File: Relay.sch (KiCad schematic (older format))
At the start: 9 parts

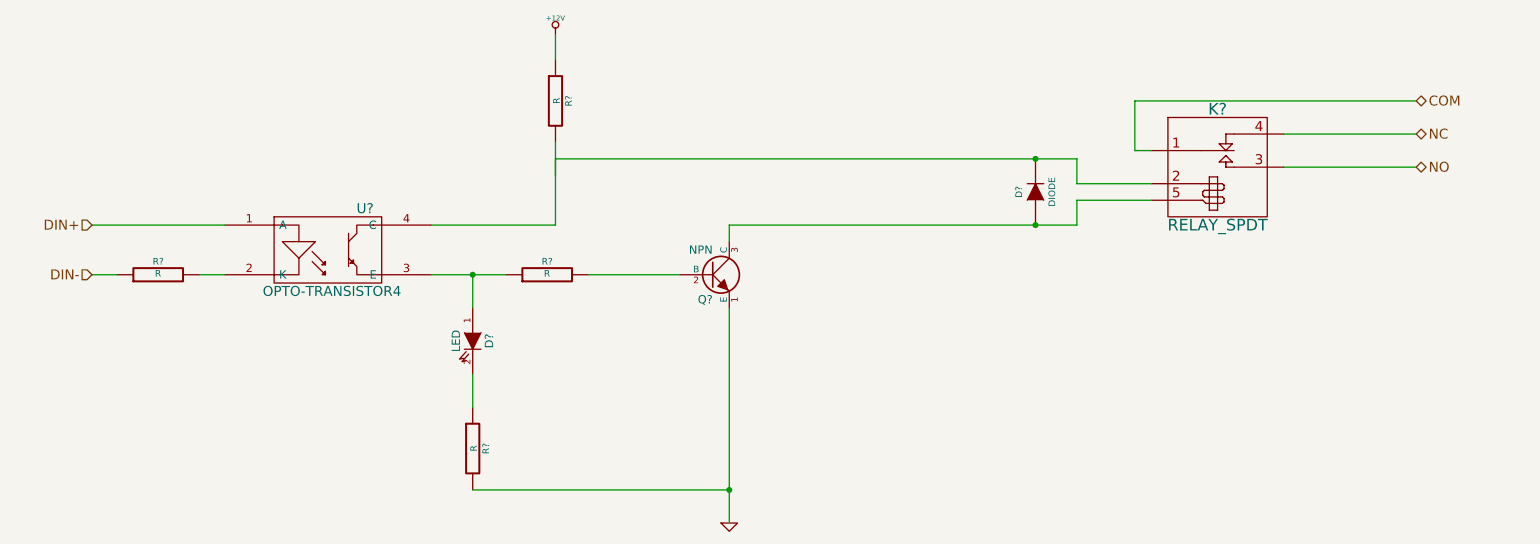
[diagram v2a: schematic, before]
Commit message: 3.9 Understanding The Arduino Module Added content to Arduino and block (header) modules
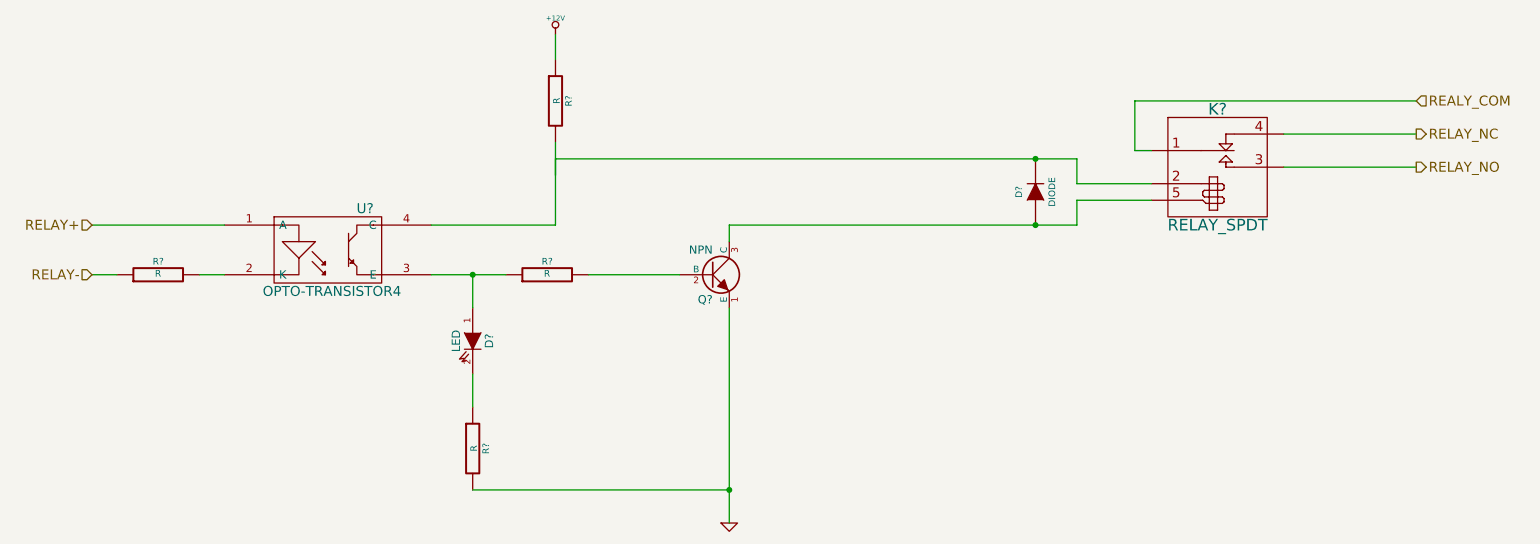
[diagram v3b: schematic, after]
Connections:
- net labels added: REALY_COM, RELAY+, RELAY-, RELAY_NC, RELAY_NO
- net labels removed: COM, DIN+, DIN-, NC, NO
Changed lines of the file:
@@
 Sheet 3 9
 Title ""
-Date "8 feb 2014"
+Date "10 feb 2014"
 Rev ""
 Comp ""
@@
 $EndDescr
 Text HLabel 1950 3400 0    60   Input ~ 0
-DIN+
+RELAY+
 Text HLabel 1950 3700 0    60   Input ~ 0
-DIN-
+RELAY-
 $Comp
 L RELAY_SPDT K?
@@
 	1    0    0    -1
 $EndComp
-Text HLabel 9950 2850 2    60   BiDi ~ 0
-NC
-Text HLabel 9950 3050 2    60   BiDi ~ 0
-NO
+Text HLabel 9950 2850 2    60   Output ~ 0
+RELAY_NC
+Text HLabel 9950 3050 2    60   Output ~ 0
+RELAY_NO
 Wire Wire Line
 	9950 2850 9150 2850
 Wire Wire Line
 	9950 3050 9150 3050
-Text HLabel 9950 2650 2    60   BiDi ~ 0
-COM
+Text HLabel 9950 2650 2    60   Input ~ 0
+REALY_COM
 Wire Wire Line
 	8350 2950 8250 2950

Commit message: 5.3 Video 1/2 Associating and Placing the Relay Module
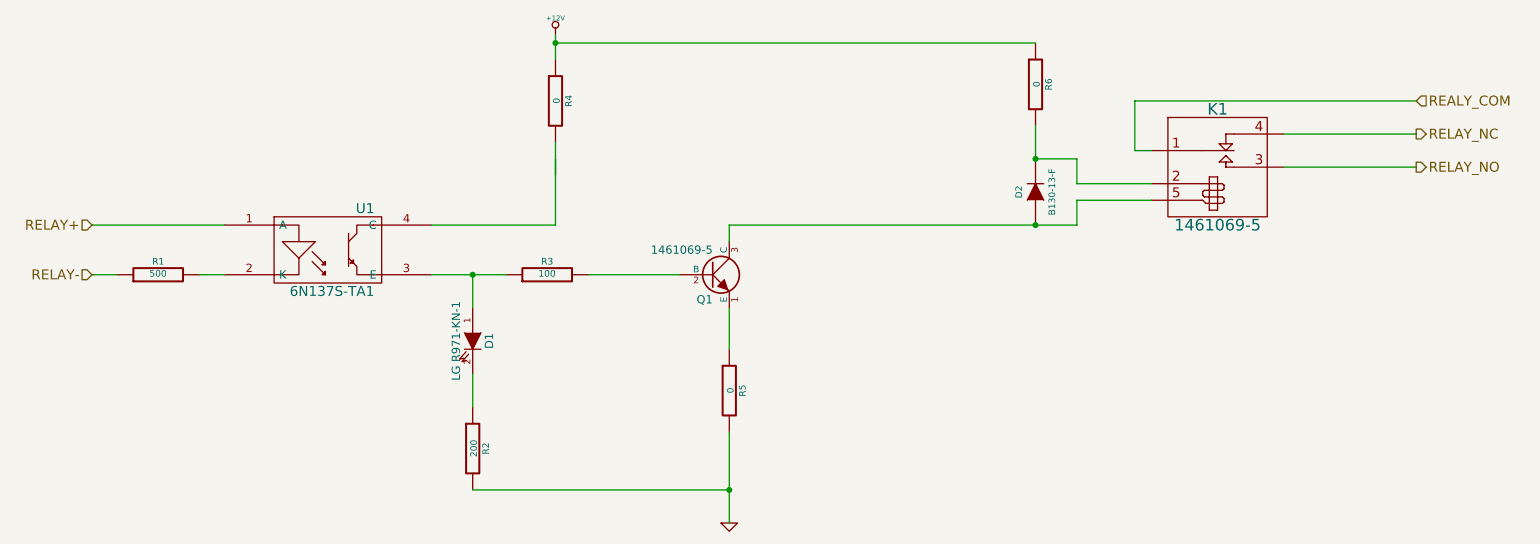
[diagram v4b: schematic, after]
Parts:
- added R5, R6: 0, ~, symbol R
- D1: renamed from D?; value LED -> LG R971-KN-1; Distributor Part Number (none) -> 475-1410-1-ND; Distributor Part Number Link (none) -> http://www.digikey.com/product-detail/en/LG%20R971-KN-1/475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; MFG Name (none) -> OSRAM Opto Semiconductors Inc
- D2: renamed from D?; value DIODE -> B130-13-F; Distributor Part Number (none) -> B130-FDICT-ND; Distributor Part Number Link (none) -> http://catalog.osram-os.com/catalogue/catalogue.do;jsession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; MFG Name (none) -> Diodes Incorporated; MFG Part Number (none) -> B130-13-F
- K1: renamed from K?; value RELAY_SPDT -> 1461069-5; Distributor Part Number (none) -> 1461069-5; Distributor Part Number Link (none) -> http://www.digikey.com/product-detail/en/1461069-5/PB1321-N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; MFG Name (none) -> Tyco
- Q1: renamed from Q?; value NPN -> 1461069-5; Distributor Part Number (none) -> PB1321-ND; Distributor Part Number Link (none) -> http://www.digikey.com/product-detail/en/1461069-5/PB1321-N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; MFG Name (none) -> TE Connectivity; MFG Part Number (none) -> 1461069-5
- R1: renamed from R?; value R -> 500
- R2: renamed from R?; value R -> 200
- R3: renamed from R?; value R -> 100
- R4: renamed from R?; value R -> 0
- U1: renamed from U?; value OPTO-TRANSISTOR4 -> 6N137S-TA1; Distributor Part Number (none) -> 160-1794-1-ND; Distributor Part Number Link (none) -> http://www.digikey.com/product-detail/en/6N137S-TA1/160-179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; MFG Name (none) -> Lite-On Inc; MFG Part Number (none) -> 6N137S-TA1
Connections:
- wire segments 29 -> 28
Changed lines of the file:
@@
 $Descr A4 11693 8268
 encoding utf-8
-Sheet 3 9
+Sheet 2 9
 Title ""
-Date "10 feb 2014"
+Date "19 feb 2014"
 Rev ""
 Comp ""
@@
 RELAY-
 $Comp
-L RELAY_SPDT K?
+L RELAY_SPDT K1
 U 1 1 52F3152B
 P 8750 2900
-F 0 "K?" H 8750 3100 70  0000 C CNN
-F 1 "RELAY_SPDT" H 8750 2400 70  0000 C CNN
+F 0 "K1" H 8750 3100 70  0000 C CNN
+F 1 "1461069-5" H 8750 2400 70  0000 C CNN
 F 2 "~" H 8750 2900 60  0000 C CNN
-F 3 "~" H 8750 2900 60  0000 C CNN
+F 3 "http://media.digikey.com/pdf/Data%20Sheets/Tyco%20Electronics%20P%20B%20PDFs/ORWH.pdf" H 8750 2900 60  0001 C CNN
+F 4 "Tyco" H 8750 2900 60  0001 C CNN "MFG Name"
+F 5 "1461069-5" H 8750 2900 60  0001 C CNN "Distributor Part Number"
+F 6 "http://www.digikey.com/product-detail/en/1461069-5/PB1321-ND/3318145" H 8750 2900 60  0001 C CNN "Distributor Part Number Link"
 	1    8750 2900
 	1    0    0    -1
@@
 	8350 2950 8250 2950
 $Comp
-L NPN Q?
+L NPN Q1
 U 1 1 52F31850
 P 5700 3700
-F 0 "Q?" H 5700 3550 50  0000 R CNN
-F 1 "NPN" H 5700 3850 50  0000 R CNN
+F 0 "Q1" H 5700 3550 50  0000 R CNN
+F 1 "1461069-5" H 5700 3850 50  0000 R CNN
 F 2 "~" H 5700 3700 60  0000 C CNN
-F 3 "~" H 5700 3700 60  0000 C CNN
+F 3 "http://www.fairchildsemi.com/ds/FM/FMBS2383.pdf" H 5700 3700 60  0001 C CNN
+F 4 "TE Connectivity" H 5700 3700 60  0001 C CNN "MFG Name"
+F 5 "1461069-5" H 5700 3700 60  0001 C CNN "MFG Part Number"
+F 6 "PB1321-ND" H 5700 3700 60  0001 C CNN "Distributor Part Number"
+F 7 "http://www.digikey.com/product-detail/en/1461069-5/PB1321-ND/3318145" H 5700 3700 60  0001 C CNN "Distributor Part Number Link"
 	1    5700 3700
 	1    0    0    -1
 $EndComp
 $Comp
-L R R?
+L R R3
 U 1 1 52F3185F
 P 4700 3700
-F 0 "R?" V 4780 3700 40  0000 C CNN
-F 1 "R" V 4707 3701 40  0000 C CNN
+F 0 "R3" V 4780 3700 40  0000 C CNN
+F 1 "100" V 4707 3701 40  0000 C CNN
 F 2 "~" V 4630 3700 30  0000 C CNN
 F 3 "~" H 4700 3700 30  0000 C CNN
@@
 	5500 3700 4950 3700
 $Comp
-L OPTO-TRANSISTOR4 U?
+L OPTO-TRANSISTOR4 U1
 U 1 1 52F3188A
 P 3400 3550
-F 0 "U?" H 3600 3800 60  0000 C CNN
-F 1 "OPTO-TRANSISTOR4" H 3400 3300 60  0000 C CNN
+F 0 "U1" H 3600 3800 60  0000 C CNN
+F 1 "6N137S-TA1" H 3400 3300 60  0000 C CNN
 F 2 "" H 3400 3550 60  0000 C CNN
-F 3 "" H 3400 3550 60  0000 C CNN
+F 3 "http://media.digikey.com/PDF/Data%20Sheets/Lite-On%20PDFs/6N137%20Series.pdf" H 3400 3550 60  0001 C CNN
+F 4 "Lite-On Inc" H 3400 3550 60  0001 C CNN "MFG Name"
+F 5 "6N137S-TA1" H 3400 3550 60  0001 C CNN "MFG Part Number"
+F 6 "160-1794-1-ND" H 3400 3550 60  0001 C CNN "Distributor Part Number"
+F 7 "http://www.digikey.com/product-detail/en/6N137S-TA1/160-1794-1-ND/1969189" H 3400 3550 60  0001 C CNN "Distributor Part Number Link"
 	1    3400 3550
 	1    0    0    -1
@@
 	2750 3400 1950 3400
 Wire Wire Line
-	4000 3700 4250 3700
-Wire Wire Line
-	4250 3700 4450 3700
-$Comp
-L LED D?
+	4000 3700 4450 3700
+$Comp
+L LED D1
 U 1 1 52F318C2
 P 4250 4100
-F 0 "D?" H 4250 4200 50  0000 C CNN
-F 1 "LED" H 4250 4000 50  0000 C CNN
+F 0 "D1" H 4250 4200 50  0000 C CNN
+F 1 "LG R971-KN-1" H 4250 4000 50  0000 C CNN
 F 2 "~" H 4250 4100 60  0000 C CNN
-F 3 "~" H 4250 4100 60  0000 C CNN
+F 3 "http://catalog.osram-os.com/catalogue/catalogue.do;jsessionid=B38D4035738FAE714C474120326E9384?act=downloadFile&favOid=02000002000009ee000100b6" H 4250 4100 60  0001 C CNN
+F 4 "OSRAM Opto Semiconductors Inc" H 4250 4100 60  0001 C CNN "MFG Name"
+F 5 "475-1410-1-ND" H 4250 4100 60  0001 C CNN "Distributor Part Number"
+F 6 "http://www.digikey.com/product-detail/en/LG%20R971-KN-1/475-1410-1-ND/1802598" H 4250 4100 60  0001 C CNN "Distributor Part Number Link"
 	1    4250 4100
 	0    1    1    0
 $EndComp
 $Comp
-L GND #PWR?
+L GND #PWR01
 U 1 1 52F318DB
 P 5800 5200
-F 0 "#PWR?" H 5800 5200 30  0001 C CNN
+F 0 "#PWR01" H 5800 5200 30  0001 C CNN
 F 1 "GND" H 5800 5130 30  0001 C CNN
 F 2 "" H 5800 5200 60  0000 C CNN
@@
 $EndComp
 Wire Wire Line
-	5800 3900 5800 5000
-Wire Wire Line
-	5800 5000 5800 5200
-Wire Wire Line
 	8250 2950 8250 2650
 Wire Wire Line
@@
 Connection ~ 4250 3700
 $Comp
-L R R?
+L R R2
 U 1 1 52F3195C
 P 4250 4750
-F 0 "R?" V 4330 4750 40  0000 C CNN
-F 1 "R" V 4257 4751 40  0000 C CNN
+F 0 "R2" V 4330 4750 40  0000 C CNN
+F 1 "200" V 4257 4751 40  0000 C CNN
 F 2 "~" V 4180 4750 30  0000 C CNN
 F 3 "~" H 4250 4750 30  0000 C CNN
@@
 	4750 2900 4750 3400
 $Comp
-L R R?
+L R R4
 U 1 1 52F319EA
 P 4750 2650
-F 0 "R?" V 4830 2650 40  0000 C CNN
-F 1 "R" V 4757 2651 40  0000 C CNN
+F 0 "R4" V 4830 2650 40  0000 C CNN
+F 1 "0" V 4757 2651 40  0000 C CNN
 F 2 "~" V 4680 2650 30  0000 C CNN
 F 3 "~" H 4750 2650 30  0000 C CNN
@@
 $EndComp
 $Comp
-L +12V #PWR?
+L +12V #PWR02
 U 1 1 52F31A0A
 P 4750 2250
-F 0 "#PWR?" H 4750 2200 20  0001 C CNN
+F 0 "#PWR02" H 4750 2200 20  0001 C CNN
 F 1 "+12V" H 4750 2350 30  0000 C CNN
 F 2 "" H 4750 2250 60  0000 C CNN
@@
 	4750 3400 4000 3400
 $Comp
-L R R?
+L R R1
 U 1 1 52F31A44
 P 2350 3700
-F 0 "R?" V 2430 3700 40  0000 C CNN
-F 1 "R" V 2357 3701 40  0000 C CNN
+F 0 "R1" V 2430 3700 40  0000 C CNN
+F 1 "500" V 2357 3701 40  0000 C CNN
 F 2 "~" V 2280 3700 30  0000 C CNN
 F 3 "~" H 2350 3700 30  0000 C CNN
@@
 	2100 3700 1950 3700
 $Comp
-L DIODE D?
+L DIODE D2
 U 1 1 52F31AA3
 P 7650 3200
-F 0 "D?" H 7650 3300 40  0000 C CNN
-F 1 "DIODE" H 7650 3100 40  0000 C CNN
+F 0 "D2" H 7650 3300 40  0000 C CNN
+F 1 "B130-13-F" H 7650 3100 40  0000 C CNN
 F 2 "~" H 7650 3200 60  0000 C CNN
-F 3 "~" H 7650 3200 60  0000 C CNN
+F 3 "http://www.diodes.com/datasheets/ds13002.pdf" H 7650 3200 60  0001 C CNN
+F 4 "Diodes Incorporated" H 7650 3200 60  0001 C CNN "MFG Name"
+F 5 "B130-13-F" H 7650 3200 60  0001 C CNN "MFG Part Number"
+F 6 "B130-FDICT-ND" H 7650 3200 60  0001 C CNN "Distributor Part Number"
+F 7 "http://catalog.osram-os.com/catalogue/catalogue.do;jsessionid=B38D4035738FAE714C474120326E9384?act=downloadFile&favOid=02000002000009ee000100b6" H 7650 3200 60  0001 C CNN "Distributor Part Number Link"
 	1    7650 3200
 	0    -1   -1   0
@@
 	7900 3250 7900 3400
 Wire Wire Line
-	4750 3000 7650 3000
-Wire Wire Line
 	7650 3000 7900 3000
 Wire Wire Line
@@
 Connection ~ 7650 3000
 Wire Wire Line
-	7900 3400 7650 3400
-Wire Wire Line
-	7650 3400 5800 3400
+	7900 3400 5800 3400
 Connection ~ 7650 3400
 Wire Wire Line
 	5800 3400 5800 3500
+$Comp
+L R R6
+U 1 1 53041CE3
+P 7650 2550
+F 0 "R6" V 7730 2550 40  0000 C CNN
+F 1 "0" V 7657 2551 40  0000 C CNN
+F 2 "~" V 7580 2550 30  0000 C CNN
+F 3 "~" H 7650 2550 30  0000 C CNN
+	1    7650 2550
+	1    0    0    -1
+$EndComp
+Wire Wire Line
+	7650 2300 4750 2300
+Connection ~ 4750 2300
+Wire Wire Line
+	7650 2800 7650 3000
+$Comp
+L R R5
+U 1 1 53041E7B
+P 5800 4400
+F 0 "R5" V 5880 4400 40  0000 C CNN
+F 1 "0" V 5807 4401 40  0000 C CNN
+F 2 "~" V 5730 4400 30  0000 C CNN
+F 3 "~" H 5800 4400 30  0000 C CNN
+	1    5800 4400
+	1    0    0    -1
+$EndComp
+Wire Wire Line
+	5800 3900 5800 4150
+Wire Wire Line
+	5800 4650 5800 5200
 $EndSCHEMATC
